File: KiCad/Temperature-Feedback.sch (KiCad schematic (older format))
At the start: 7 parts, among them J2 Thermocouple Terminal Block, U4 MCP617

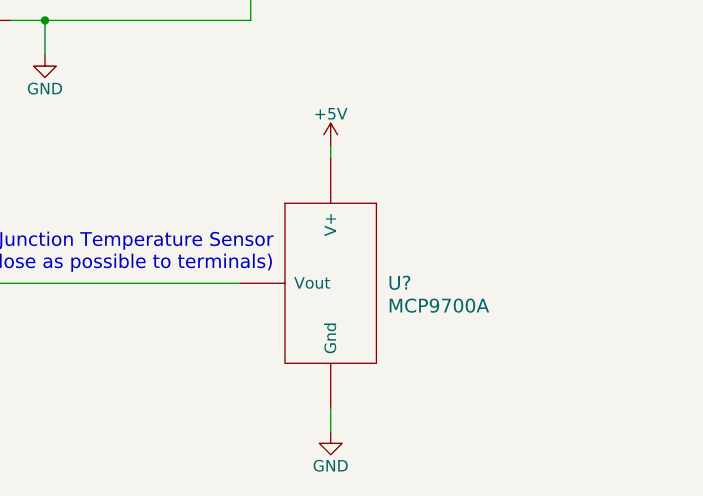
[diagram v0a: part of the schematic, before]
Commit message: aluminum components added to BOM and kicad library for 7-seg ICs
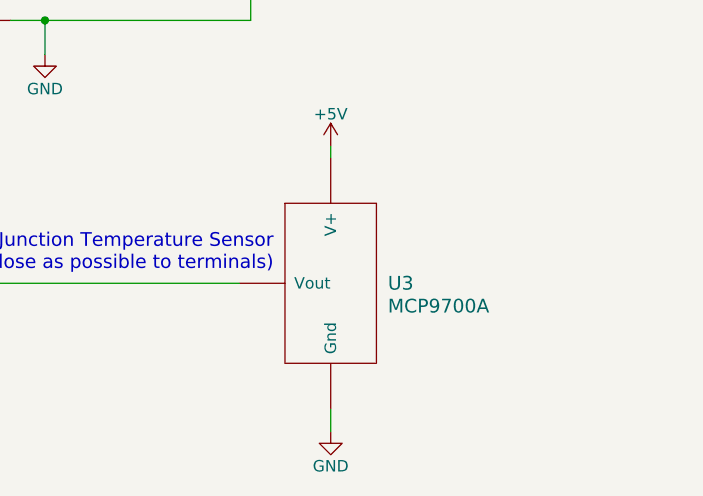
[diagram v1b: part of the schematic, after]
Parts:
- gave numbers to parts that had none: 1
- renumbered J2 to J4
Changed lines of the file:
@@
 $EndComp
 $Comp
-L CONN_01X04 J2
+L CONN_01X04 J4
 U 1 1 564E7E06
 P 8800 3050
-F 0 "J2" H 8800 3300 50  0000 C CNN
+F 0 "J4" H 8800 3300 50  0000 C CNN
 F 1 "Thermocouple Terminal Block" V 8900 3050 50  0000 C CNN
 F 2 "" H 8800 3050 60  0000 C CNN
@@
 Connection ~ 6050 3700
 $Comp
-L MCP9700A U?
+L MCP9700A U3
 U 1 1 564E89FE
 P 8600 4950
-F 0 "U?" H 8850 4950 60  0000 L CNN
+F 0 "U3" H 8850 4950 60  0000 L CNN
 F 1 "MCP9700A" H 8850 4850 60  0000 L CNN
 F 2 "" H 8600 4950 60  0000 C CNN

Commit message: nichrome mounting parts added to bom and feedback terminal block removed
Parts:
- removed J4: Thermocouple Terminal Block, symbol CONN_01X04
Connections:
- net labels removed: Kn1, Kn2
- wire segments 33 -> 25
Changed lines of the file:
@@
 	0    1    1    0
-$EndComp
-$Comp
-L CONN_01X04 J4
-U 1 1 564E7E06
-P 8800 3050
-F 0 "J4" H 8800 3300 50  0000 C CNN
-F 1 "Thermocouple Terminal Block" V 8900 3050 50  0000 C CNN
-F 2 "" H 8800 3050 60  0000 C CNN
-F 3 "" H 8800 3050 60  0000 C CNN
-	1    8800 3050
-	1    0    0    -1
 $EndComp
 Wire Wire Line
@@
 Connection ~ 7350 3600
 Wire Wire Line
-	8600 2900 8400 2900
-Wire Wire Line
-	8400 2900 8400 2300
-Wire Wire Line
 	8400 2300 6700 2300
 Wire Wire Line
-	6100 2500 8250 2500
-Wire Wire Line
-	8250 2500 8250 3000
-Wire Wire Line
-	8250 3000 8600 3000
-Wire Wire Line
-	8600 3100 8100 3100
-Wire Wire Line
-	8100 3100 8100 3600
-Wire Wire Line
-	8100 3600 7800 3600
-Wire Wire Line
-	7200 3800 8250 3800
-Wire Wire Line
-	8250 3800 8250 3200
-Wire Wire Line
-	8250 3200 8600 3200
+	8450 3600 7800 3600
 $Comp
 L GND #PWR?
@@
 Wire Wire Line
 	6250 2500 6250 2600
-Connection ~ 6250 2500
 Wire Wire Line
 	7350 3800 7350 3950
-Connection ~ 7350 3800
-Text Label 8400 2900 0    60   ~ 0
-Kp1
-Text Label 8400 3000 0    60   ~ 0
-Kn1
-Text Label 8400 3100 0    60   ~ 0
-Kp2
-Text Label 8400 3200 0    60   ~ 0
-Kn2
 Text HLabel 3700 2400 0    60   Output ~ 0
 Tk1
@@
 Cold Junction Temperature Sensor\n(place as close as possible to terminals)
 Wire Notes Line
-	9100 2900 9700 2900
+	8700 2300 9300 2300
 Wire Notes Line
-	9700 2900 9800 3000
+	9300 2300 9400 2400
 Wire Notes Line
-	9800 3000 9900 2900
+	9400 2400 9500 2300
 Wire Notes Line
-	9900 2900 10000 3000
+	9500 2300 9600 2400
 Wire Notes Line
-	10000 3000 10100 2900
+	9600 2400 9700 2300
 Wire Notes Line
-	10100 2900 10150 2950
+	9700 2300 9750 2350
 Wire Notes Line
-	10150 2950 10100 3000
+	9750 2350 9700 2400
 Wire Notes Line
-	10100 3000 10000 2900
+	9700 2400 9600 2300
 Wire Notes Line
-	10000 2900 9900 3000
+	9600 2300 9500 2400
 Wire Notes Line
-	9900 3000 9800 2900
+	9500 2400 9400 2300
 Wire Notes Line
-	9800 2900 9700 3000
+	9400 2300 9300 2400
 Wire Notes Line
-	9700 3000 9100 3000
+	9300 2400 8700 2400
 Wire Notes Line
-	9100 3100 9700 3100
+	8850 3600 9450 3600
 Wire Notes Line
-	9700 3100 9800 3200
+	9450 3600 9550 3700
 Wire Notes Line
-	9800 3200 9900 3100
+	9550 3700 9650 3600
 Wire Notes Line
-	9900 3100 10000 3200
+	9650 3600 9750 3700
 Wire Notes Line
-	10000 3200 10100 3100
+	9750 3700 9850 3600
 Wire Notes Line
-	10100 3100 10150 3150
+	9850 3600 9900 3650
 Wire Notes Line
-	10150 3150 10100 3200
+	9900 3650 9850 3700
 Wire Notes Line
-	10100 3200 10000 3100
+	9850 3700 9750 3600
 Wire Notes Line
-	10000 3100 9900 3200
+	9750 3600 9650 3700
 Wire Notes Line
-	9900 3200 9800 3100
+	9650 3700 9550 3600
 Wire Notes Line
-	9800 3100 9700 3200
+	9550 3600 9450 3700
 Wire Notes Line
-	9700 3200 9100 3200
+	9450 3700 8850 3700
+Wire Wire Line
+	7200 3800 7350 3800
+Wire Wire Line
+	6100 2500 6250 2500
+Text HLabel 8400 2300 2    60   Input ~ 0
+Kp1
+Text HLabel 8450 3600 2    60   Input ~ 0
+Kp2
+Wire Notes Line
+	8700 2400 8700 2550
+Wire Notes Line
+	8600 2550 8800 2550
+Wire Notes Line
+	8650 2600 8750 2600
+Wire Notes Line
+	8850 3700 8850 3850
+Wire Notes Line
+	8750 3850 8950 3850
+Wire Notes Line
+	8800 3900 8900 3900
 $EndSCHEMATC

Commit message: updated temperature feedback schematic
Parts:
- removed Rf1, Rf3: 100, symbol R
- removed Rf2, Rf4: 16.5k, symbol R
- added R? (x5): R, symbol R
- added U?: MCP41050, symbol MCP41050
- U4: symbol LMC6062 -> LMC6062-RESCUE-Easy-PCB
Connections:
- net Tk1 is gone; now on net Tref: U4.1
- net +5V: now also R?.1, U?.8 (Vdd)
- net GND: now also R?.2, U?.4 (Vss); no longer U4.2 (-), U4.6 (-)
- net Tref: now also R?.2; no longer U3.~ (Vout)
- net at U4.3 (+): now also U3.~ (Vout)
- net K+: now reaches U4.5 (+)
- net Tk2 renamed Tk
- net Tk: now also U?.7 (PB0)
- new net: R?.1, R?.2, U4.2 (-)
- new net: R?.2, U4.6 (-), U?.6 (PW0)
- new net MOSI: U?.3 (SI)
- new net SCK: U?.2 (SCK)
- new net Vref-: R?.1, R?.1, R?.1, R?.2
- new net ~POT: U?.1 (~CS)
- no-connect marks 0 -> 1
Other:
- moved on the sheet: U3, U4A, U4B
